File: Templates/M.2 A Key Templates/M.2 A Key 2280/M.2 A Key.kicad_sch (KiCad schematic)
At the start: 2 parts

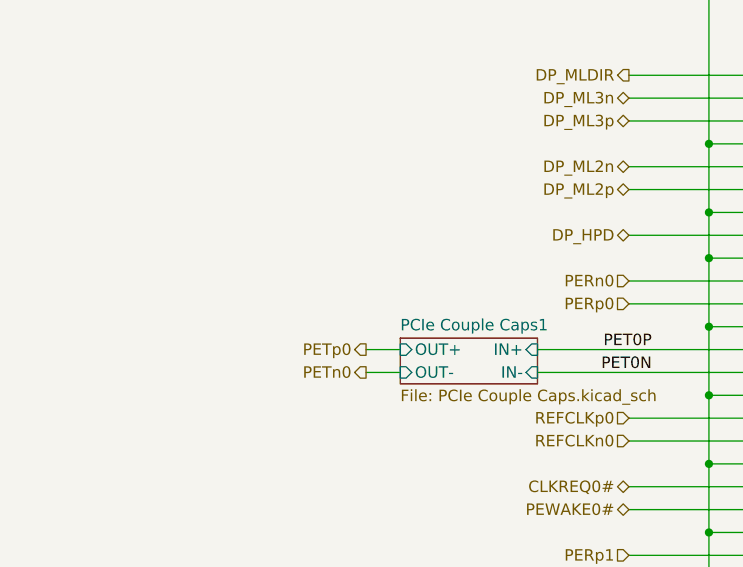
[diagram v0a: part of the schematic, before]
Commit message: Added AC Cap note to A Key Templates
added note about AC coupling caps for diff signals on the a key templates
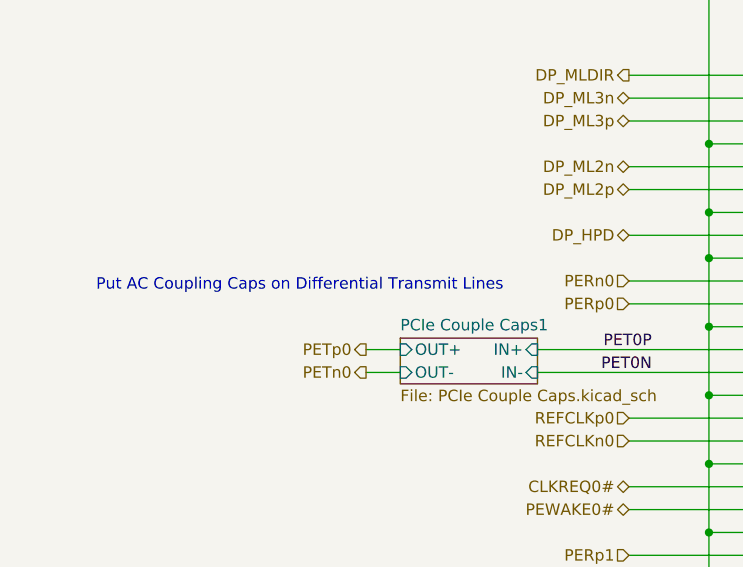
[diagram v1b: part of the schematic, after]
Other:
- note added: "Put AC Coupling Caps on Differential Transmit Lines"
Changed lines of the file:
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@@
 	(generator_version "9.0")
 	(paper "A4")
+	(text "Put AC Coupling Caps on Differential Transmit Lines"
+		(exclude_from_sim no)
+		(at 48.514 90.678 0)
+		(effects
+			(font
+				(size 1.27 1.27)
+			)
+		)
+	)
 	(junction
 		(at 93.98 102.87)
